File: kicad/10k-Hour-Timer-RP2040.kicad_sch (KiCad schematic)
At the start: 15 parts, among them J1 Conn_01x03_Pin, J2 JST_SH_SM03B, J3 USB_C_Receptacle_USB2.0_16P, U1 USBLC6-2SC6

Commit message: floorplanning
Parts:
- added JP24: SolderJumper_2_Open, Jumper:SolderJumper-2_P1.3mm_Open_RoundedPad1.0x1.5mm, symbol Jumper:SolderJumper_2_Open
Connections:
- net GND: now also JP24.2 (B)
- net at J3.S1 (SHIELD), JP1.1 (A): now also JP24.1 (A)
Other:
- moved on the sheet: TP1
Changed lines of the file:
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@@
 	)
 	(junction
-		(at 73.66 72.39)
+		(at 73.66 71.12)
 		(diameter 0)
 		(color 0 0 0 0)
@@
 	)
 	(junction
+		(at 50.8 95.25)
+		(diameter 0)
+		(color 0 0 0 0)
+	)
+	(junction
 		(at 58.42 95.25)
 		(diameter 0)
@@
 	(wire
 		(pts
+			(xy 60.96 95.25) (xy 58.42 95.25)
+		)
+		(stroke
+			(width 0)
+			(type default)
+		)
+	)
+	(wire
+		(pts
 			(xy 59.69 146.05) (xy 73.66 146.05)
 		)
@@
 	(wire
 		(pts
+			(xy 50.8 95.25) (xy 50.8 97.79)
+		)
+		(stroke
+			(width 0)
+			(type default)
+		)
+	)
+	(wire
+		(pts
 			(xy 210.82 147.32) (xy 184.15 147.32)
 		)
@@
 	(wire
 		(pts
+			(xy 58.42 100.33) (xy 58.42 97.79)
+		)
+		(stroke
+			(width 0)
+			(type default)
+		)
+	)
+	(wire
+		(pts
 			(xy 184.15 142.24) (xy 215.9 142.24)
 		)
@@
 	(wire
 		(pts
-			(xy 73.66 69.85) (xy 73.66 72.39)
+			(xy 73.66 69.85) (xy 73.66 71.12)
 		)
 		(stroke
@@
 	(wire
 		(pts
+			(xy 97.79 71.12) (xy 97.79 73.66)
+		)
+		(stroke
+			(width 0)
+			(type default)
+		)
+	)
+	(wire
+		(pts
 			(xy 123.19 57.15) (xy 125.73 57.15)
 		)
@@
 	(wire
 		(pts
+			(xy 60.96 97.79) (xy 58.42 97.79)
+		)
+		(stroke
+			(width 0)
+			(type default)
+		)
+	)
+	(wire
+		(pts
 			(xy 88.9 63.5) (xy 92.71 63.5)
 		)
@@
 	(wire
 		(pts
-			(xy 73.66 73.66) (xy 73.66 72.39)
+			(xy 73.66 71.12) (xy 73.66 72.39)
 		)
 		(stroke
@@
 	(wire
 		(pts
-			(xy 73.66 73.66) (xy 97.79 73.66)
+			(xy 73.66 71.12) (xy 97.79 71.12)
 		)
 		(stroke
@@
 	)
 	(label "USB_In_D-"
-		(at 77.47 73.66 0)
+		(at 77.47 71.12 0)
 		(effects
 			(font
@@
 					(size 1.27 1.27)
 				)
+				(hide yes)
 			)
 		)
@@
 	)
 	(symbol
+		(lib_id "Jumper:SolderJumper_2_Open")
+		(at 54.61 97.79 0)
+		(unit 1)
+		(exclude_from_sim no)
+		(in_bom no)
+		(on_board yes)
+		(dnp no)
+		(property "Reference" "JP24"
+			(at 54.61 100.33 0)
+			(effects
+				(font
+					(size 1.27 1.27)
+				)
+				(hide yes)
+			)
+		)
+		(property "Value" "SolderJumper_2_Open"
+			(at 39.624 103.124 0)
+			(effects
+				(font
+					(size 1.27 1.27)
+				)
+				(hide yes)
+			)
+		)
+		(property "Footprint" "Jumper:SolderJumper-2_P1.3mm_Open_RoundedPad1.0x1.5mm"
+			(at 54.61 97.79 0)
+			(effects
+				(font
+					(size 1.27 1.27)
+				)
+				(hide yes)
+			)
+		)
+		(property "Datasheet" "~"
+			(at 54.61 97.79 0)
+			(effects
+				(font
+					(size 1.27 1.27)
+				)
+				(hide yes)
+			)
+		)
+		(property "Description" "Solder Jumper, 2-pole, open"
+			(at 54.61 97.79 0)
+			(effects
+				(font
+					(size 1.27 1.27)
+				)
+				(hide yes)
+			)
+		)
+		(property "Subsystem" "01A-USB"
+			(at 54.61 97.79 0)
+			(effects
+				(font
+					(size 1.27 1.27)
+				)
+				(hide yes)
+			)
+		)
+		(property "MPN" "(Embedded)"
+			(at 54.61 97.79 0)
+			(effects
+				(font
+					(size 1.27 1.27)
+				)
+				(hide yes)
+			)
+		)
+		(pin "1"
+		)
+		(pin "2"
+		)
+		(instances
+			(project "10k-Hour-Timer-RP2040"
+				(path "/9d26b66f-2a94-42e5-8460-016e0bf95186"
+					(reference "JP24")
+					(unit 1)
+				)
+			)
+		)
+	)
+	(symbol
 		(lib_id "Connector:TestPoint")
 		(at 132.08 57.15 0)
@@
 	(symbol
 		(lib_id "Connector:TestPoint")
-		(at 58.42 95.25 270)
+		(at 60.96 95.25 270)
 		(unit 1)
 		(exclude_from_sim no)
@@
 		(dnp no)
 		(property "Reference" "TP1"
-			(at 62.738 95.504 90)
+			(at 65.278 95.504 90)
 			(effects
 				(font
@@
 		)
 		(property "Value" "GND"
-			(at 63.5 93.9801 90)
+			(at 66.04 93.9801 90)
 			(effects
 				(font
@@
 		)
 		(property "Footprint" "project footprints:TestPoint_THTPad_D2.0mm_Drill1.0mm"
-			(at 58.42 100.33 0)
+			(at 60.96 100.33 0)
 			(effects
 				(font
@@
 		)
 		(property "Datasheet" "~"
-			(at 58.42 100.33 0)
+			(at 60.96 100.33 0)
 			(effects
 				(font
@@
 		)
 		(property "Description" "test point"
-			(at 58.42 95.25 0)
+			(at 60.96 95.25 0)
 			(effects
 				(font
@@
 		)
 		(property "Subsystem" "01A-USB"
-			(at 58.42 95.25 90)
+			(at 60.96 95.25 90)
 			(effects
 				(font
@@
 		)
 		(property "MPN" "(Embedded)"
-			(at 58.42 95.25 90)
+			(at 60.96 95.25 90)
 			(effects
 				(font
@@
 	(symbol
 		(lib_id "power:PWR_FLAG")
-		(at 58.42 97.79 270)
+		(at 60.96 97.79 270)
 		(unit 1)
 		(exclude_from_sim no)
@@
 		(fields_autoplaced yes)
 		(property "Reference" "#FLG02"
-			(at 60.325 97.79 0)
+			(at 62.865 97.79 0)
 			(effects
 				(font
@@
 		)
 		(property "Value" "PWR_FLAG"
-			(at 62.23 97.7899 90)
+			(at 64.77 97.7899 90)
 			(effects
 				(font
@@
 		)
 		(property "Footprint" ""
-			(at 58.42 97.79 0)
+			(at 60.96 97.79 0)
 			(effects
 				(font
@@
 		)
 		(property "Datasheet" "~"
-			(at 58.42 97.79 0)
+			(at 60.96 97.79 0)
 			(effects
 				(font
@@
 		)
 		(property "Description" "Special symbol for telling ERC where power comes from"
-			(at 58.42 97.79 0)
+			(at 60.96 97.79 0)
 			(effects
 				(font
@@
 	(symbol
 		(lib_id "power:GND")
-		(at 58.42 97.79 0)
+		(at 58.42 100.33 0)
 		(unit 1)
 		(exclude_from_sim no)
@@
 		(dnp no)
 		(property "Reference" "#PWR03"
-			(at 58.42 104.14 0)
+			(at 58.42 106.68 0)
 			(effects
 				(font
@@
 		)
 		(property "Value" "GND"
-			(at 58.42 101.854 0)
+			(at 58.166 104.394 0)
 			(effects
 				(font
@@
 		)
 		(property "Footprint" ""
-			(at 58.42 97.79 0)
+			(at 58.42 100.33 0)
 			(effects
 				(font
@@
 		)
 		(property "Datasheet" ""
-			(at 58.42 97.79 0)
+			(at 58.42 100.33 0)
 			(effects
 				(font
@@
 		)
 		(property "Description" "Power symbol creates a global label with name \"GND\" , ground"
-			(at 58.42 97.79 0)
+			(at 58.42 100.33 0)
 			(effects
 				(font

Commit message: buzzer fp, power mux layout
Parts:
- U1: now not fitted; now left out of the parts list
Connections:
- net USB_In_D+ is gone; now on net USB_D+: J3.A6 (D+), J3.B6 (D+), U1.3 (I/O2)
- net USB_In_D- is gone; now on net USB_D-: J3.A7 (D-), J3.B7 (D-), U1.1 (I/O1)
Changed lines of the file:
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@@
+	)
+	(junction
+		(at 97.79 76.2)
+		(diameter 0)
+		(color 0 0 0 0)
 	)
 	(junction
@@
 		(color 0 0 0 0)
 	)
+	(junction
+		(at 97.79 73.66)
+		(diameter 0)
+		(color 0 0 0 0)
+	)
 	(no_connect
 		(at 73.66 87.63)
@@
 	(wire
 		(pts
+			(xy 97.79 76.2) (xy 107.95 76.2)
+		)
+		(stroke
+			(width 0)
+			(type default)
+		)
+	)
+	(wire
+		(pts
 			(xy 210.82 62.23) (xy 210.82 101.6)
 		)
@@
 		(pts
 			(xy 60.96 97.79) (xy 58.42 97.79)
+		)
+		(stroke
+			(width 0)
+			(type default)
+		)
+	)
+	(wire
+		(pts
+			(xy 97.79 73.66) (xy 107.95 73.66)
 		)
 		(stroke
@@
 		(unit 1)
 		(exclude_from_sim no)
-		(in_bom yes)
-		(on_board yes)
-		(dnp no)
+		(in_bom no)
+		(on_board no)
+		(dnp yes)
 		(property "Reference" "U1"
 			(at 103.124 69.596 0)

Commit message: layout floorplanning
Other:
- added sheet TM1638_Display (TM1638_Display.kicad_sch)
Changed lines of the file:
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@@
+	)
+	(sheet
+		(at 88.9 165.1)
+		(size 34.29 26.67)
+		(exclude_from_sim no)
+		(in_bom yes)
+		(on_board yes)
+		(dnp no)
+		(fields_autoplaced yes)
+		(stroke
+			(width 0.1524)
+			(type solid)
+		)
+		(fill
+			(color 0 0 0 0.0000)
+		)
+		(property "Sheetname" "TM1638_Display"
+			(at 88.9 164.3884 0)
+			(effects
+				(font
+					(size 1.27 1.27)
+				)
+				(justify left bottom)
+			)
+		)
+		(property "Sheetfile" "TM1638_Display.kicad_sch"
+			(at 88.9 192.3546 0)
+			(effects
+				(font
+					(size 1.27 1.27)
+				)
+				(justify left top)
+			)
+		)
+		(instances
+			(project "10k-Hour-Timer-RP2040"
+				(path "/9d26b66f-2a94-42e5-8460-016e0bf95186"
+					(page "5")
+				)
+			)
+		)
 	)
 	(sheet

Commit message: floorplanning
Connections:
- net VBUS_IN: now reaches C1.1, FB1.1, J3.A4 (VBUS), J3.A9 (VBUS), J3.B4 (VBUS), J3.B9 (VBUS), TP2.1, U1.5 (VBUS)
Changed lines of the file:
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@@
+		)
+	)
+	(label "VBUS_IN"
+		(at 81.28 57.15 0)
+		(effects
+			(font
+				(size 1.27 1.27)
+			)
+			(justify left bottom)
 		)
 	)

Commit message: layout - 7seg display
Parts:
- added H1, H2, H3, H4: MH-4.7mm, project footprints:MountingHole_4.7mm, symbol Mechanical:MountingHole

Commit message: layout - footprints update - may have corrupted kicad_sch project lib
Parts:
- added BOM3: Coin Vibration Motor 3V, symbol Project_Library:BOM_PLACEHOLDER
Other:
- sheet MCU-IO ports: added DISP_CLK, DISP_DIO, DISP_STB, VBAT_VBUS; removed none
- sheet Power-DCDC-Charger-Battery ports: added VBAT_VBUS; removed none
- sheet RTC ports: added VBAT_VBUS; removed none
- sheet TM1638_Display ports: added DISP_CLK, DISP_DIO, DISP_STB, VBAT_VBUS; removed none
- moved on the sheet: C1, C2, FB1, J1, J2, J3, R1, R2, TP1, TP2, TP3, U1

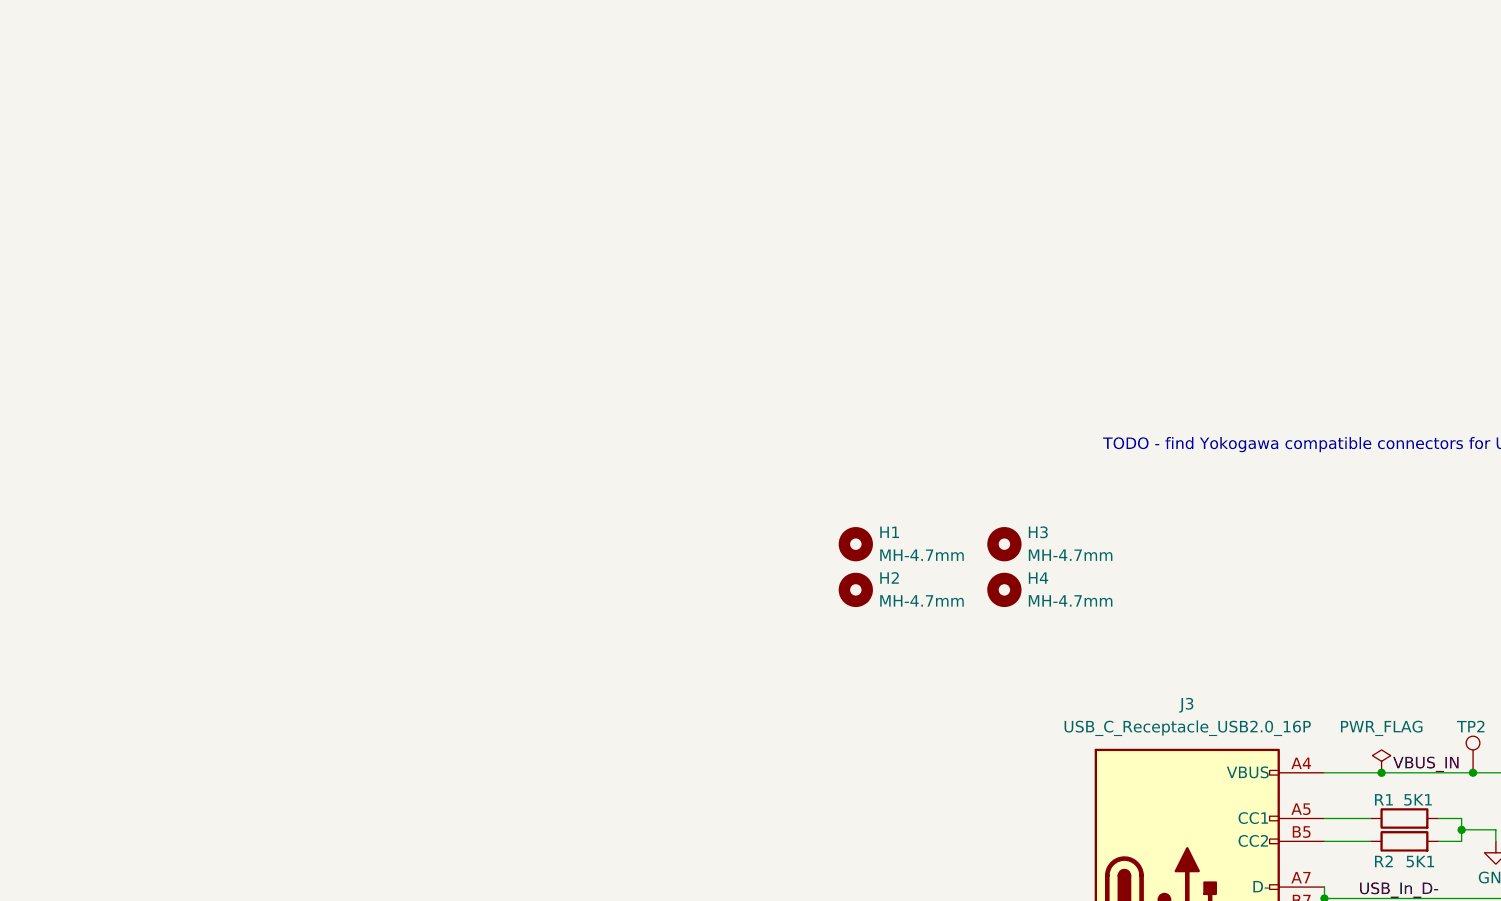
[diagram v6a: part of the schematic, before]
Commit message: changed usb port, prepare first bom export
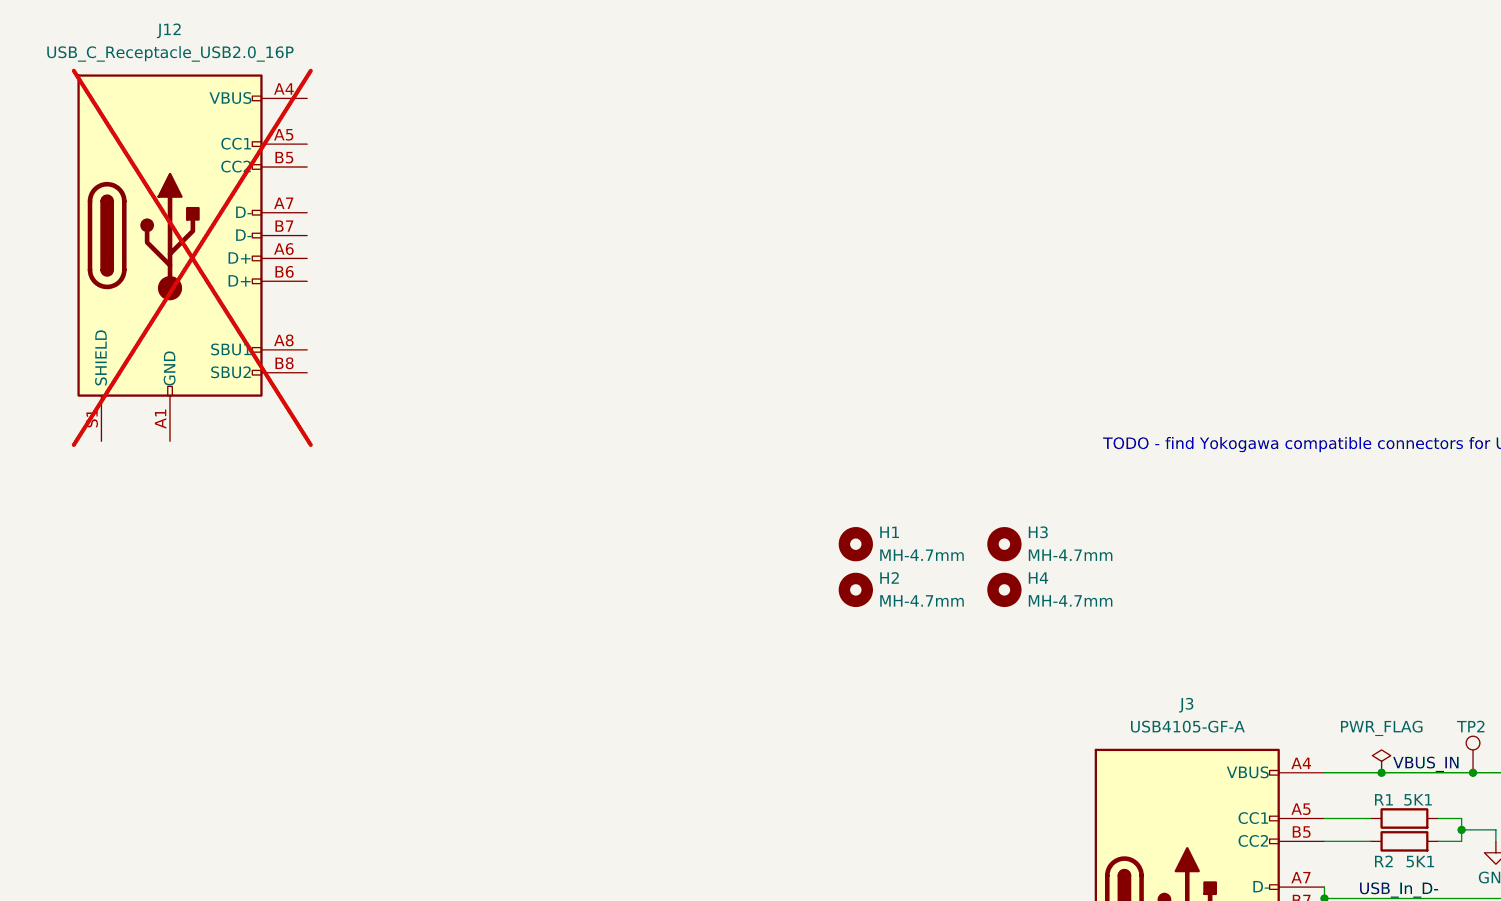
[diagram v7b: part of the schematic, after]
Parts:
- added J12: USB_C_Receptacle_USB2.0_16P, project footprints:USB_C_Receptacle_JAE_DX07S016JA1R1500, symbol Connector:USB_C_Receptacle_USB2.0_16P
- C1, C2, J1: Lab_In_Stock (none) -> Y
- J3: value USB_C_Receptacle_USB2.0_16P -> USB4105-GF-A; footprint project footprints:USB_C_Receptacle_JAE_DX07S016JA1R1500 -> project footprints:GCT_USB4105-GF-A; Lab_In_Stock (none) -> Y; MPN DX07S016JA1R1500 -> USB4105-GF-A; Manufacturer JAE Electronics -> GCT; Supplier 1 LCSC -> Digikey; Supplier 1 SKU C3197885 -> 2073-USB4105-GF-ACT-ND; Supplier 1 URL https://lcsc.com/product-detail/USB-Connectors_JAE-Electron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 -> https://www.digikey.jp/en/products/detail/gct/USB4105-GF-A/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
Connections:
- new net: J12.A1 (GND), J12.A12 (GND), J12.B1 (GND), J12.B12 (GND)
- new net: J12.A4 (VBUS), J12.A9 (VBUS), J12.B4 (VBUS), J12.B9 (VBUS)
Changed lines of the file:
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@@
+	)
+	(symbol
+		(lib_id "Connector:USB_C_Receptacle_USB2.0_16P")
+		(at -58.42 -17.78 0)
+		(unit 1)
+		(exclude_from_sim no)
+		(in_bom no)
+		(on_board no)
+		(dnp yes)
+		(fields_autoplaced yes)
+		(property "Reference" "J12"
+			(at -58.42 -40.64 0)
+			(effects
+				(font
+					(size 1.27 1.27)
+				)
+			)
+		)
+		(property "Value" "USB_C_Receptacle_USB2.0_16P"
+			(at -58.42 -38.1 0)
+			(effects
+				(font
+					(size 1.27 1.27)
+				)
+			)
+		)
+		(property "Footprint" "project footprints:USB_C_Receptacle_JAE_DX07S016JA1R1500"
+			(at -54.61 -17.78 0)
+			(effects
+				(font
+					(size 1.27 1.27)
+				)
+				(hide yes)
+			)
+		)
+		(property "Datasheet" "https://www.usb.org/sites/default/files/documents/usb_type-c.zip"
+			(at -54.61 -17.78 0)
+			(effects
+				(font
+					(size 1.27 1.27)
+				)
+				(hide yes)
+			)
+		)
+		(property "Description" "USB 2.0-only 16P Type-C Receptacle connector"
+			(at -58.42 -17.78 0)
+			(effects
+				(font
+					(size 1.27 1.27)
+				)
+				(hide yes)
+			)
+		)
+		(property "MPN" "DX07S016JA1R1500"
+			(at -58.42 -17.78 0)
+			(effects
+				(font
+					(size 1.27 1.27)
+				)
+				(hide yes)
+			)
+		)
+		(property "Manufacturer" "JAE Electronics"
+			(at -58.42 -17.78 0)
+			(effects
+				(font
+					(size 1.27 1.27)
+				)
+				(hide yes)
+			)
+		)
+		(property "Supplier 1" "LCSC"
+			(at -58.42 -17.78 0)
+			(effects
+				(font
+					(size 1.27 1.27)
+				)
+				(hide yes)
+			)
+		)
+		(property "Supplier 1 URL" "https://lcsc.com/product-detail/USB-Connectors_JAE-Electronics-DX07S016JA1R1500_C3197885.html"
+			(at -58.42 -17.78 0)
+			(effects
+				(font
+					(size 1.27 1.27)
+				)
+				(hide yes)
+			)
+		)
+		(property "Supplier 1 SKU" "C3197885"
+			(at -58.42 -17.78 0)
+			(effects
+				(font
+					(size 1.27 1.27)
+				)
+				(hide yes)
+			)
+		)
+		(property "Package" ""
+			(at -58.42 -17.78 0)
+			(effects
+				(font
+					(size 1.27 1.27)
+				)
+				(hide yes)
+			)
+		)
+		(property "Subsystem" "01A-USB"
+			(at -58.42 -17.78 0)
+			(effects
+				(font
+					(size 1.27 1.27)
+				)
+				(hide yes)
+			)
+		)
+		(pin "A9"
+		)
+		(pin "A4"
+		)
+		(pin "B4"
+		)
+		(pin "B9"
+		)
+		(pin "B5"
+		)
+		(pin "A5"
+		)
+		(pin "B8"
+		)
+		(pin "A7"
+		)
+		(pin "B6"
+		)
+		(pin "B12"
+		)
+		(pin "B7"
+		)
+		(pin "A8"
+		)
+		(pin "A1"
+		)
+		(pin "S1"
+		)
+		(pin "A6"
+		)
+		(pin "B1"
+		)
+		(pin "A12"
+		)
+		(instances
+			(project "10k-Hour-Timer-RP2040"
+				(path "/9d26b66f-2a94-42e5-8460-016e0bf95186"
+					(reference "J12")
+					(unit 1)
+				)
+			)
+		)
 	)
 	(symbol
@@
 			)
 		)
+		(property "Lab_In_Stock" "Y"
+			(at 105.41 45.72 0)
+			(effects
+				(font
+					(size 1.27 1.27)
+				)
+				(hide yes)
+			)
+		)
 		(pin "2"
 		)
@@
 			)
 		)
+		(property "Lab_In_Stock" "Y"
+			(at 44.45 125.73 0)
+			(effects
+				(font
+					(size 1.27 1.27)
+				)
+				(hide yes)
+			)
+		)
 		(pin "3"
 		)
@@
 			)
 		)
+		(property "Lab_In_Stock" "Y"
+			(at 121.92 45.72 0)
+			(effects
+				(font
+					(size 1.27 1.27)
+				)
+				(hide yes)
+			)
+		)
 		(pin "2"
 		)
@@
 			)
 		)
-		(property "Value" "USB_C_Receptacle_USB2.0_16P"
+		(property "Value" "USB4105-GF-A"
 			(at 54.61 36.83 0)
 			(effects
@@
 			)
 		)
-		(property "Footprint" "project footprints:USB_C_Receptacle_JAE_DX07S016JA1R1500"
+		(property "Footprint" "project footprints:GCT_USB4105-GF-A"
 			(at 58.42 57.15 0)
 			(effects
@@
 			)
 		)
-		(property "Datasheet" "https://www.usb.org/sites/default/files/documents/usb_type-c.zip"
+		(property "Datasheet" ""
 			(at 58.42 57.15 0)
 			(effects
@@
 			)
 		)
-		(property "Description" "USB 2.0-only 16P Type-C Receptacle connector"
+		(property "Description" "CONN RCP USB2.0 TYP C 24P SMD RA"
 			(at 54.61 57.15 0)
 			(effects
@@
 			)
 		)
-		(property "MPN" "DX07S016JA1R1500"
+		(property "MPN" "USB4105-GF-A"
 			(at 54.61 57.15 0)
 			(effects
@@
 			)
 		)
-		(property "Manufacturer" "JAE Electronics"
+		(property "Manufacturer" "GCT"
 			(at 54.61 57.15 0)
 			(effects
@@
 			)
 		)
-		(property "Supplier 1" "LCSC"
+		(property "Supplier 1" "Digikey"
 			(at 54.61 57.15 0)
 			(effects
@@
 			)
 		)
-		(property "Supplier 1 URL" "https://lcsc.com/product-detail/USB-Connectors_JAE-Electronics-DX07S016JA1R1500_C3197885.html"
+		(property "Supplier 1 URL" "https://www.digikey.jp/en/products/detail/gct/USB4105-GF-A/11198441"
 			(at 54.61 57.15 0)
 			(effects
@@
 			)
 		)
-		(property "Supplier 1 SKU" "C3197885"
+		(property "Supplier 1 SKU" "2073-USB4105-GF-ACT-ND"
 			(at 54.61 57.15 0)
 			(effects
@@
 			(at 54.61 57.15 0)
 			(effects
+				(font
+					(size 1.27 1.27)
+				)
+				(hide yes)
+			)
+		)
+		(property "Lab_In_Stock" "Y"
+			(at 54.61 57.15 0)
+			(effects

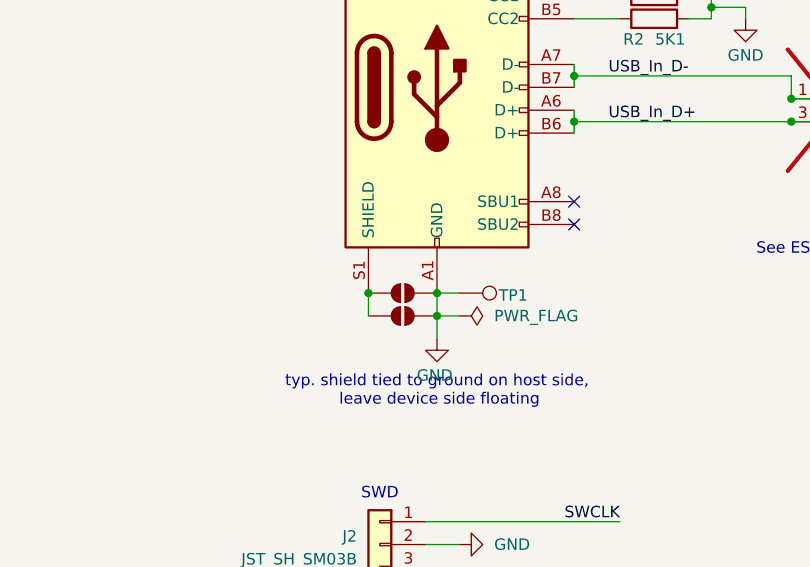
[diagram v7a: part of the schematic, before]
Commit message: DRC to zero errors - still need to check FPs
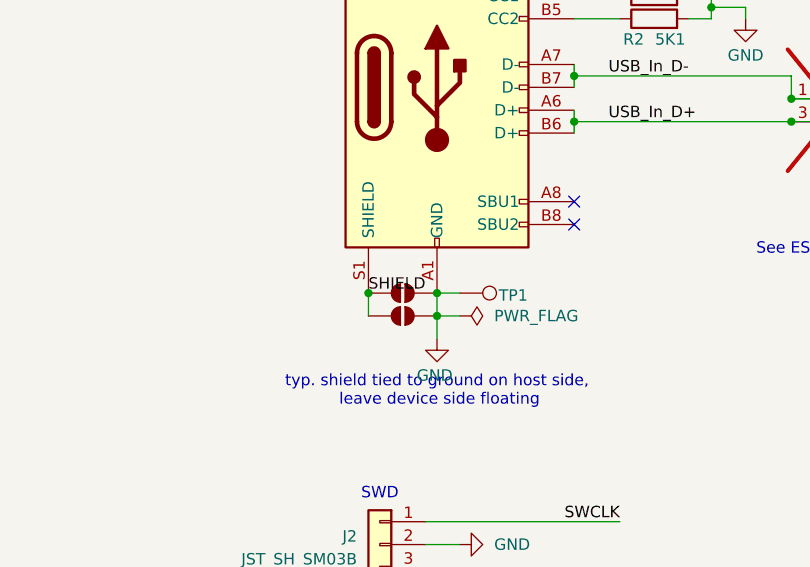
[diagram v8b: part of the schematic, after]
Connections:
- net SHIELD: now reaches J3.S1 (SHIELD), JP1.1 (A), JP24.1 (A)
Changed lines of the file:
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@@
+		)
+	)
+	(label "SHIELD"
+		(at 46.99 80.01 0)
+		(effects
+			(font
+				(size 1.27 1.27)
+			)
+			(justify left bottom)
 		)
 	)
